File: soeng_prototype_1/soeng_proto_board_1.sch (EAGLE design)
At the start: 19 parts, among them J1 2172034-1, T1 2N2222

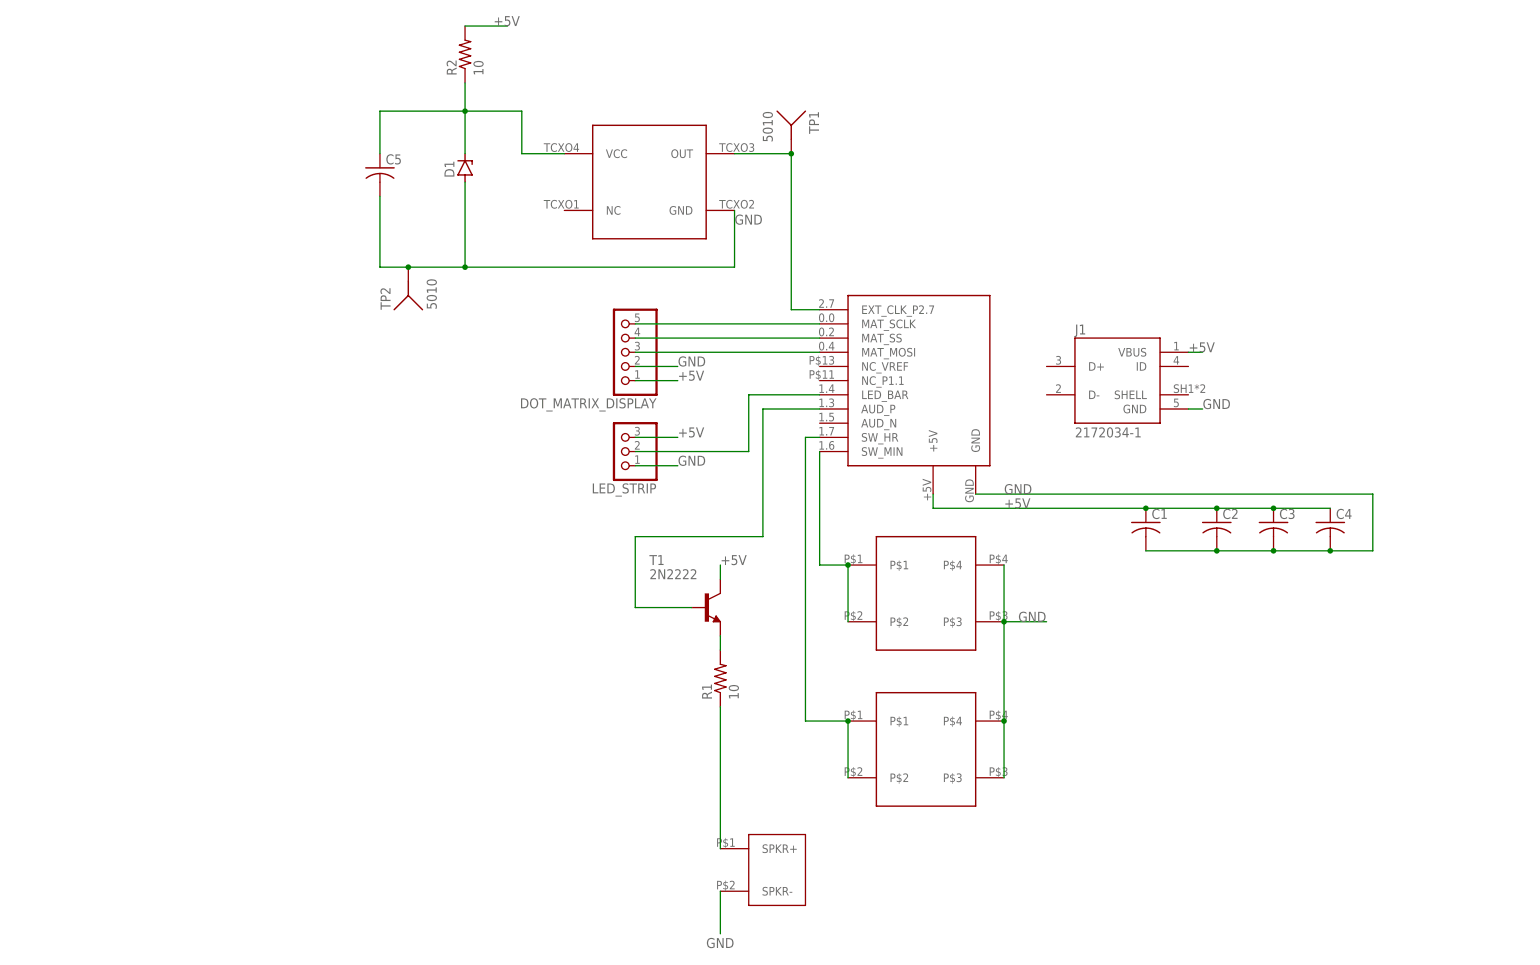
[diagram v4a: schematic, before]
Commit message: V4.1 sent out for fab.  Changed oscillator, added level shifters
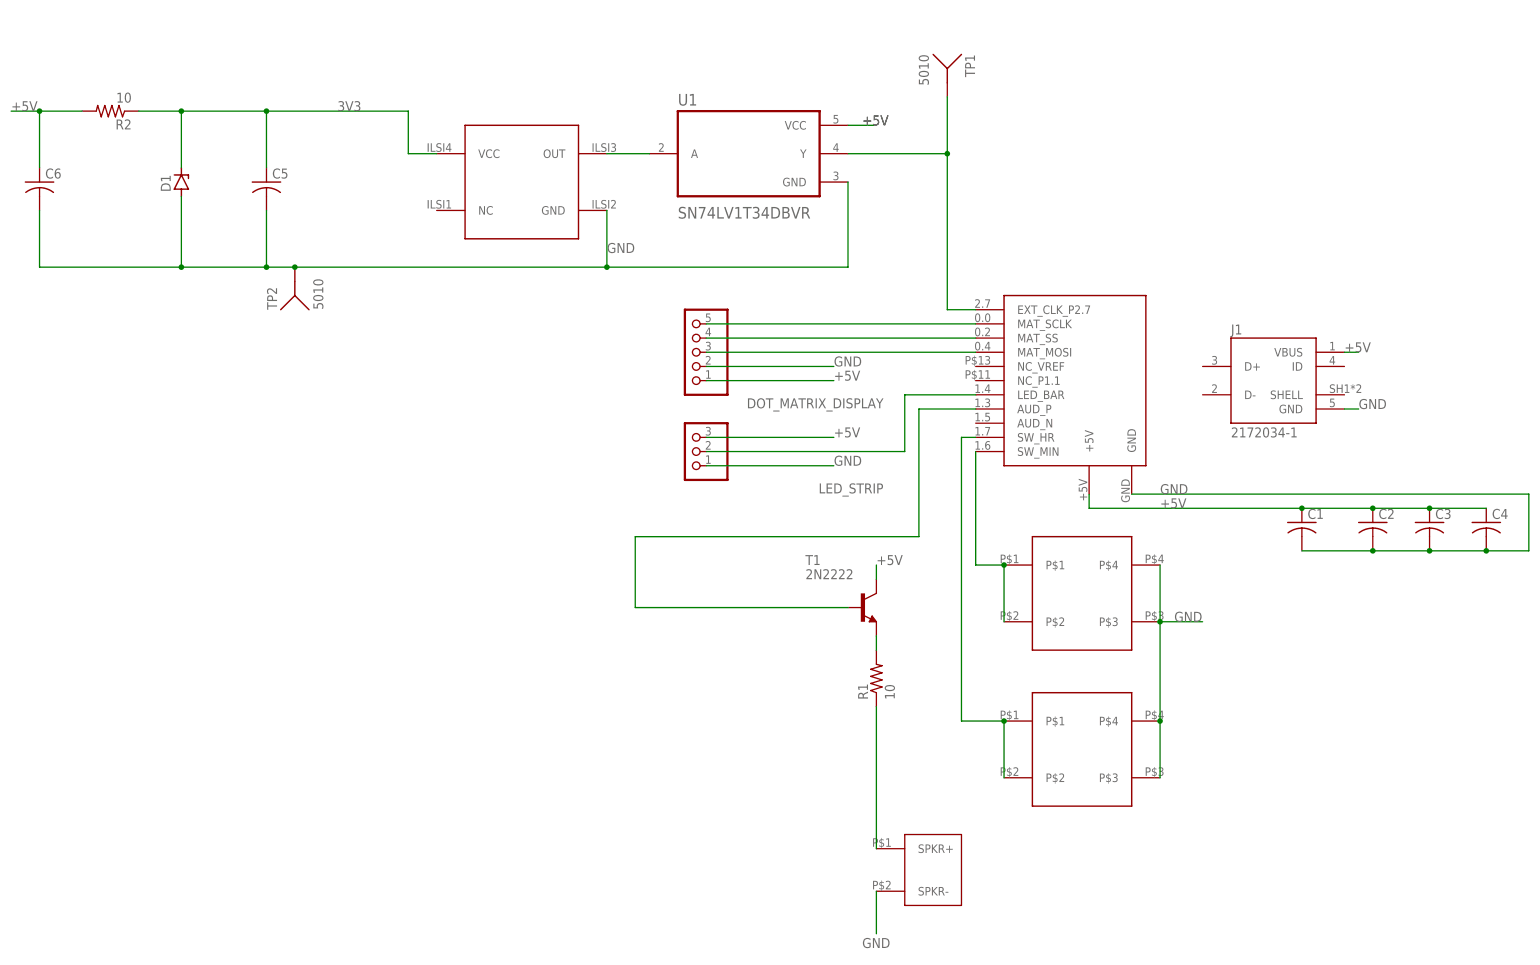
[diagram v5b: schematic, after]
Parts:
- added C6: (no value), adafruit:C-US025-025X050
- added U1: SN74LV1T34DBVR, SN74LV1T34DBVR:SN74LV1T34DBVR
- D1: device diode:ZENER-DIODEDO34-7 -> diode:ZENER-DIODEZD-10
- U$5: value TXEAPLSANF -> ILSI-I538; device lap_2019:TXEAPLSANF -> lap_2019:ILSI-I538
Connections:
- net N$11 renamed 3V3
- new net N$11: U$5.OUT, U1.A
- net +5V: now also C6.1, U1.VCC
- net GND: now also C6.2, U1.GND
- net N$10: now also U1.Y; no longer U$5.OUT
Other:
- moved on the sheet: C1, C2, C3, C4, C5, D1, DOT_MATRIX_DISPLAY, J1, LED_STRIP, R1, R2, T1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
